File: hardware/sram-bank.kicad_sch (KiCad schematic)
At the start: 9 parts, among them U1 74LVC138A, U13 74LVC138A

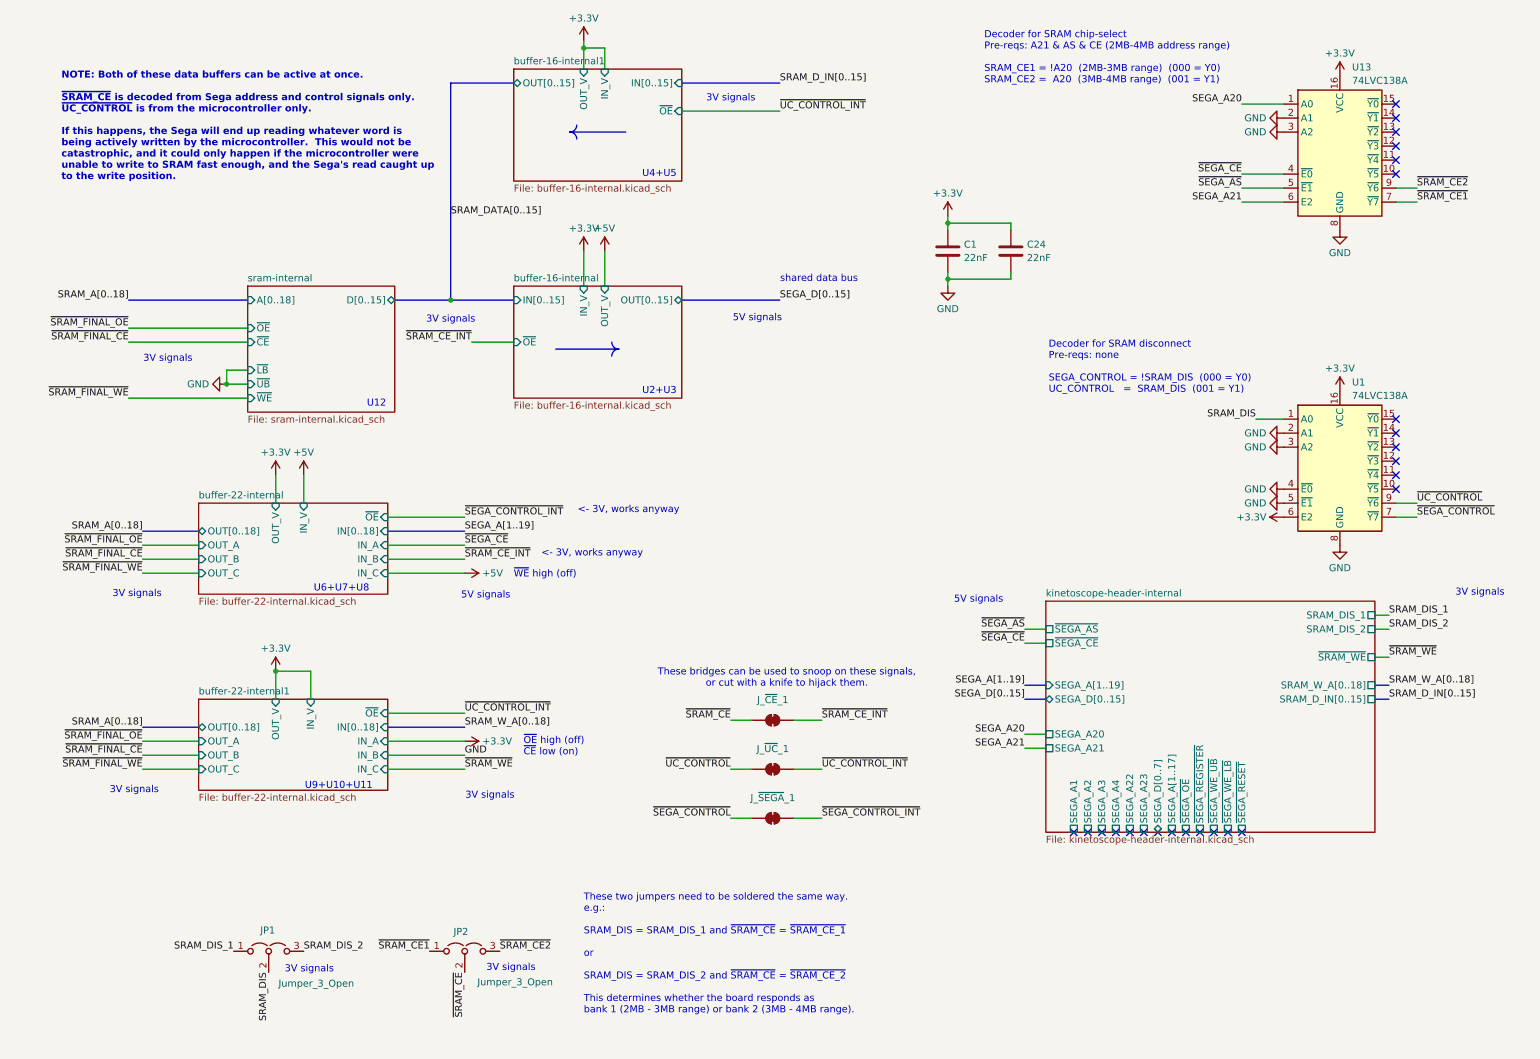
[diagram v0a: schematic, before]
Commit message: Fix SRAM bank hardware design
 - Fix SRAM OE line (was previously CE by accident)
 - Fix buffer OE line
 - Add test pads for ~{SEGA_OE}, ~{SRAM_WE}, ~{SRAM_FINAL_OE}
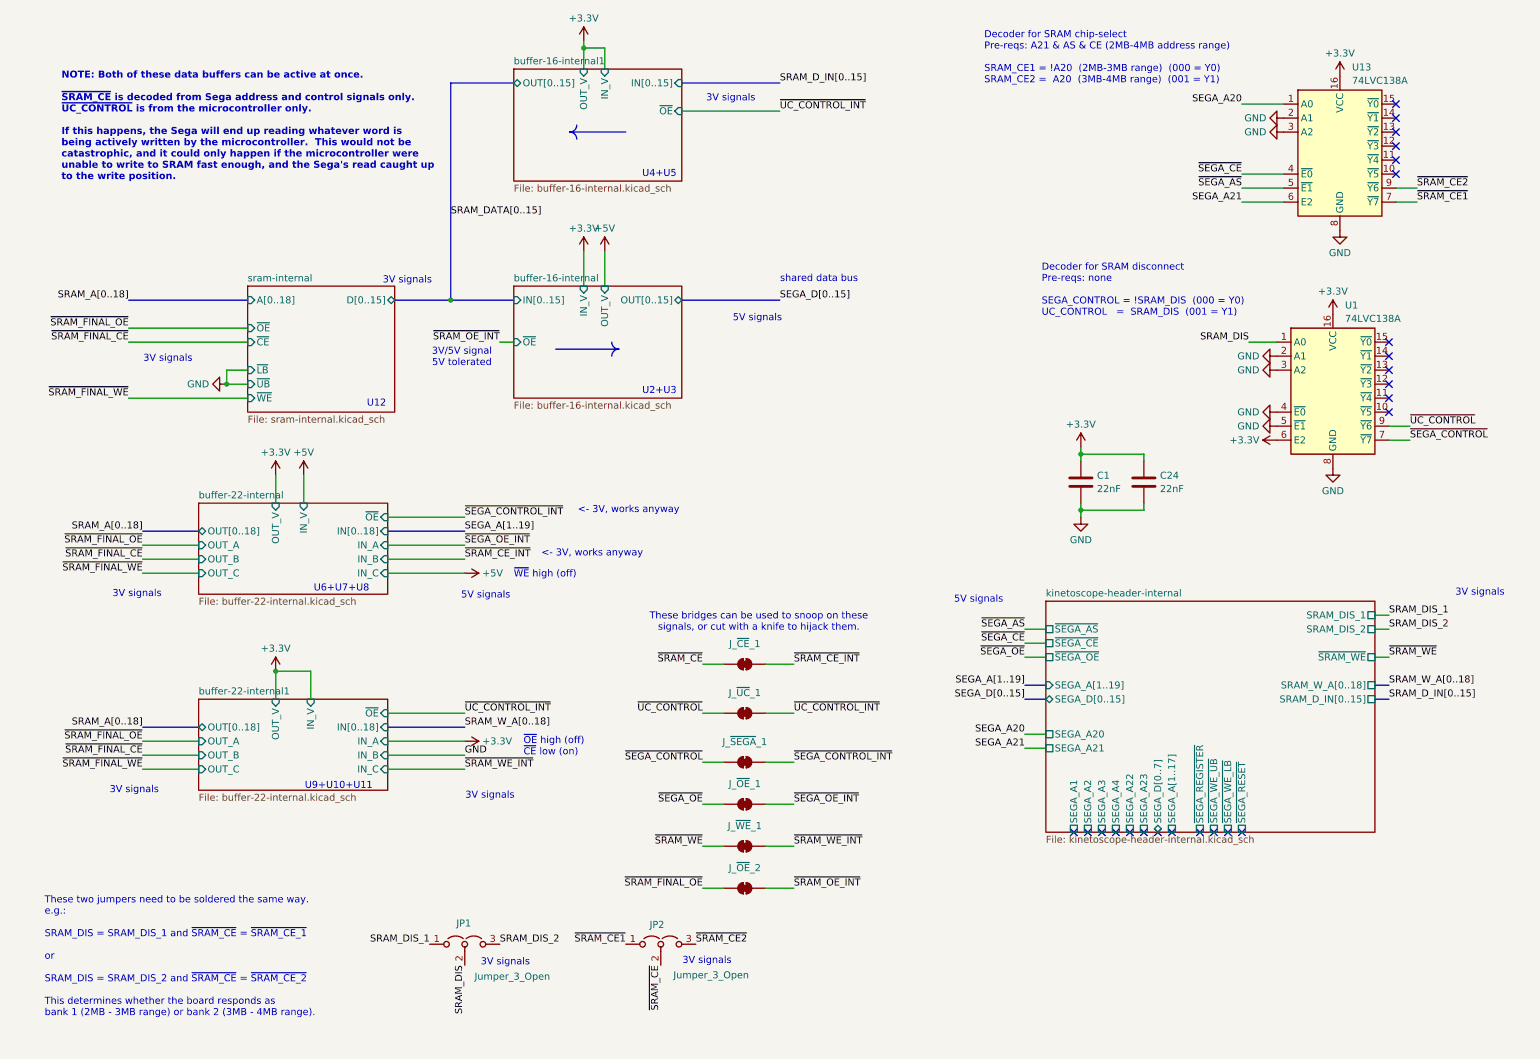
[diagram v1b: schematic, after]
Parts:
- added J_~{OE}_1, J_~{OE}_2, J_~{WE}_1: ~, Jumper:SolderJumper-2_P1.3mm_Bridged_RoundedPad1.0x1.5mm, symbol Jumper:SolderJumper_2_Bridged
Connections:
- net ~{SRAM_FINAL_OE}: now also J_~{OE}_2.1 (A)
- net ~{SRAM_WE}: now also J_~{WE}_1.1 (A)
- new net ~{SEGA_OE_INT}: J_~{OE}_1.2 (B)
- new net ~{SEGA_OE}: J_~{OE}_1.1 (A)
- new net ~{SRAM_OE_INT}: J_~{OE}_2.2 (B)
- new net ~{SRAM_WE_INT}: J_~{WE}_1.2 (B)
- no-connect marks 25 -> 24
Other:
- note added: "3V/5V signal 5V tolerated"
- moved on the sheet: C1, C24, JP1, JP2, J_~{CE}_1, J_~{SEGA}_1, J_~{UC}_1, U1

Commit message: Be consistent with SRAM bank numbering (0-1, not 1-2)
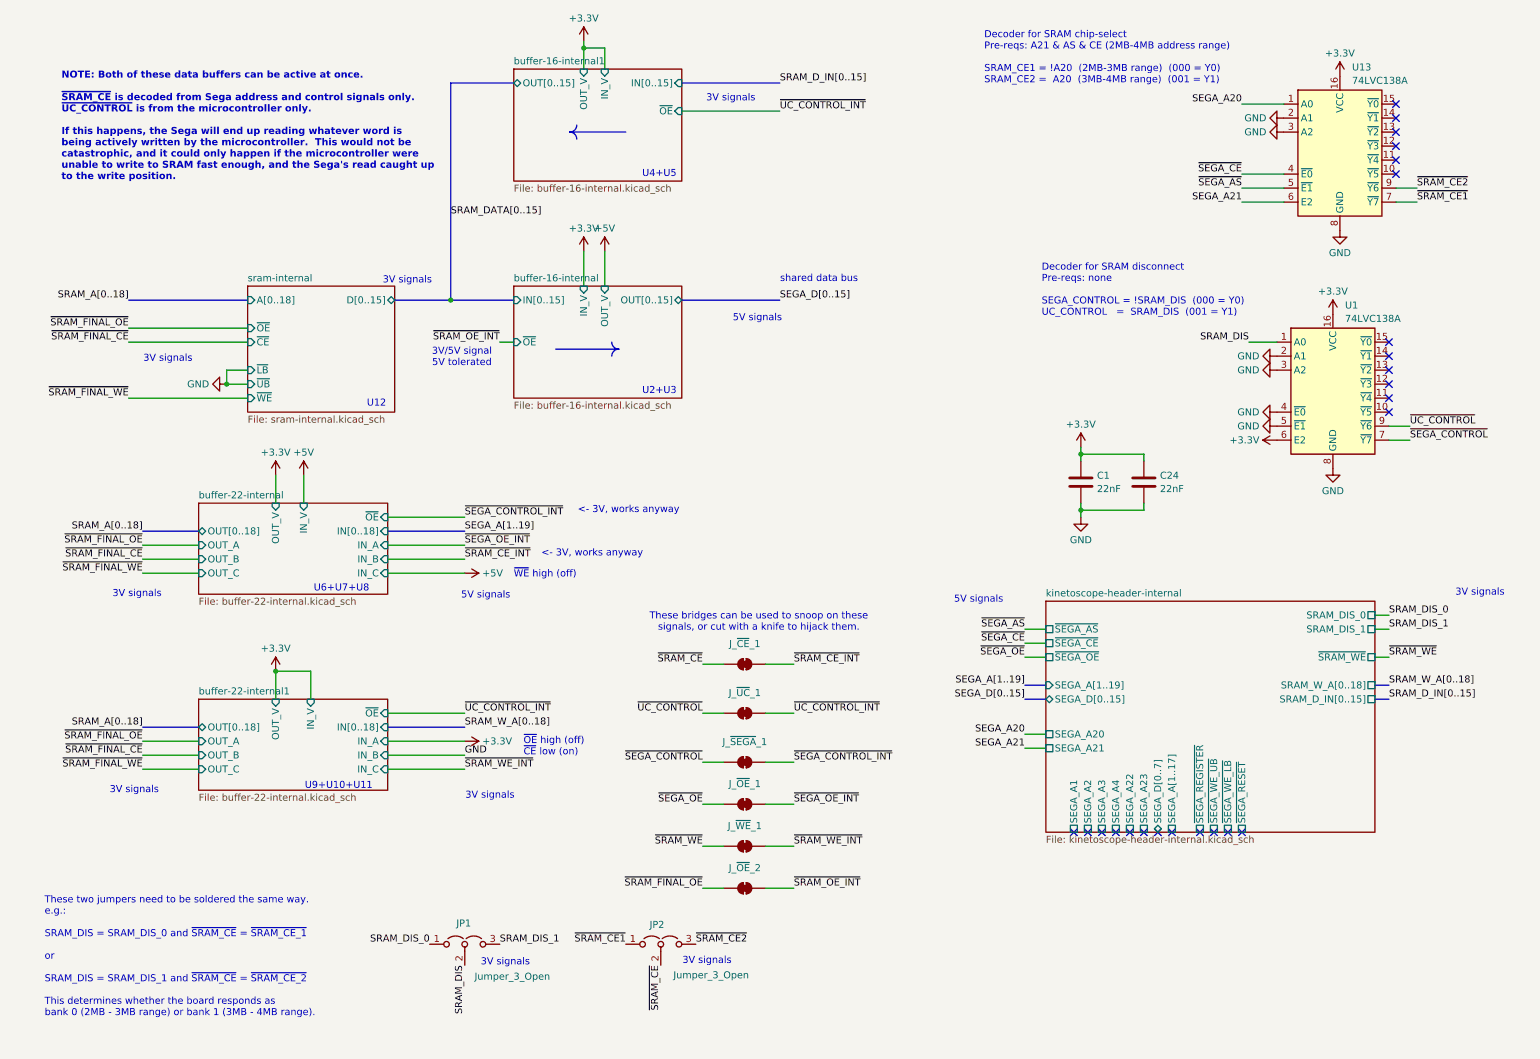
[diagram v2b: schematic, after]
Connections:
- net SRAM_DIS_2 is gone; now on net SRAM_DIS_1: JP1.3 (B)
- net SRAM_DIS_1: no longer JP1.1 (A)
- new net SRAM_DIS_0: JP1.1 (A)
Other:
- sheet kinetoscope-header-internal ports: added SRAM_DIS_0; removed SRAM_DIS_2
- note added: "These two jumpers need to be soldered the same way. e.g.: SRAM_DIS = SRAM_DIS_0 and ~{SRAM_CE} = ~{SRAM_CE_1} or SRAM_DIS = SRAM_DIS_1 and ~{SRAM_CE} = ~{SRAM_CE_2} This determines whether the board responds as bank 0 (2MB - 3MB range) or bank 1 (3MB - 4MB range)."
- note removed: "These two jumpers need to be soldered the same way. e.g.: SRAM_DIS = SRAM_DIS_1 and ~{SRAM_CE} = ~{SRAM_CE_1} or SRAM_DIS = SRAM_DIS_2 and ~{SRAM_CE} = ~{SRAM_CE_2} This determines whether the board responds as bank 1 (2MB - 3MB range) or bank 2 (3MB - 4MB range)."
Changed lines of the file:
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@@
 		)
 	)
-	(text "These two jumpers need to be soldered the same way.\ne.g.:\n\nSRAM_DIS = SRAM_DIS_1 and ~{SRAM_CE} = ~{SRAM_CE_1}\n\nor\n\nSRAM_DIS = SRAM_DIS_2 and ~{SRAM_CE} = ~{SRAM_CE_2}\n\nThis determines whether the board responds as\nbank 1 (2MB - 3MB range) or bank 2 (3MB - 4MB range)."
+	(text "These two jumpers need to be soldered the same way.\ne.g.:\n\nSRAM_DIS = SRAM_DIS_0 and ~{SRAM_CE} = ~{SRAM_CE_1}\n\nor\n\nSRAM_DIS = SRAM_DIS_1 and ~{SRAM_CE} = ~{SRAM_CE_2}\n\nThis determines whether the board responds as\nbank 0 (2MB - 3MB range) or bank 1 (3MB - 4MB range)."
 		(exclude_from_sim no)
 		(at 17.78 183.896 0)
@@
 		)
 	)
-	(label "SRAM_DIS_2"
+	(label "SRAM_DIS_1"
 		(at 261.62 124.46 0)
 		(fields_autoplaced yes)
@@
 		)
 	)
-	(label "SRAM_DIS_1"
+	(label "SRAM_DIS_0"
 		(at 261.62 121.92 0)
 		(fields_autoplaced yes)
@@
 		)
 	)
-	(label "SRAM_DIS_1"
+	(label "SRAM_DIS_0"
 		(at 87.63 181.61 180)
 		(fields_autoplaced yes)
@@
 		)
 	)
-	(label "SRAM_DIS_2"
+	(label "SRAM_DIS_1"
 		(at 100.33 181.61 0)
 		(fields_autoplaced yes)
@@
 			)
 		)
-		(pin "SRAM_DIS_2" passive
+		(pin "SRAM_DIS_1" passive
 			(at 259.08 124.46 0)
 			(effects
@@
 			)
 		)
-		(pin "SRAM_DIS_1" passive
+		(pin "SRAM_DIS_0" passive
 			(at 259.08 121.92 0)
 			(effects

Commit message: Fix SRAM bank design
 - Fix address decoders, Y0/Y1 and Y7/Y6 were flipped
 - SRAM_CE signal was insufficient, combined CE+OE needed
 - Buffer voltage at 5V meant 3.3V signals were too low, fixed to 3.3V
 - Update comments and add drawings

Only updates schematic.  PCB update will come in a later commit.
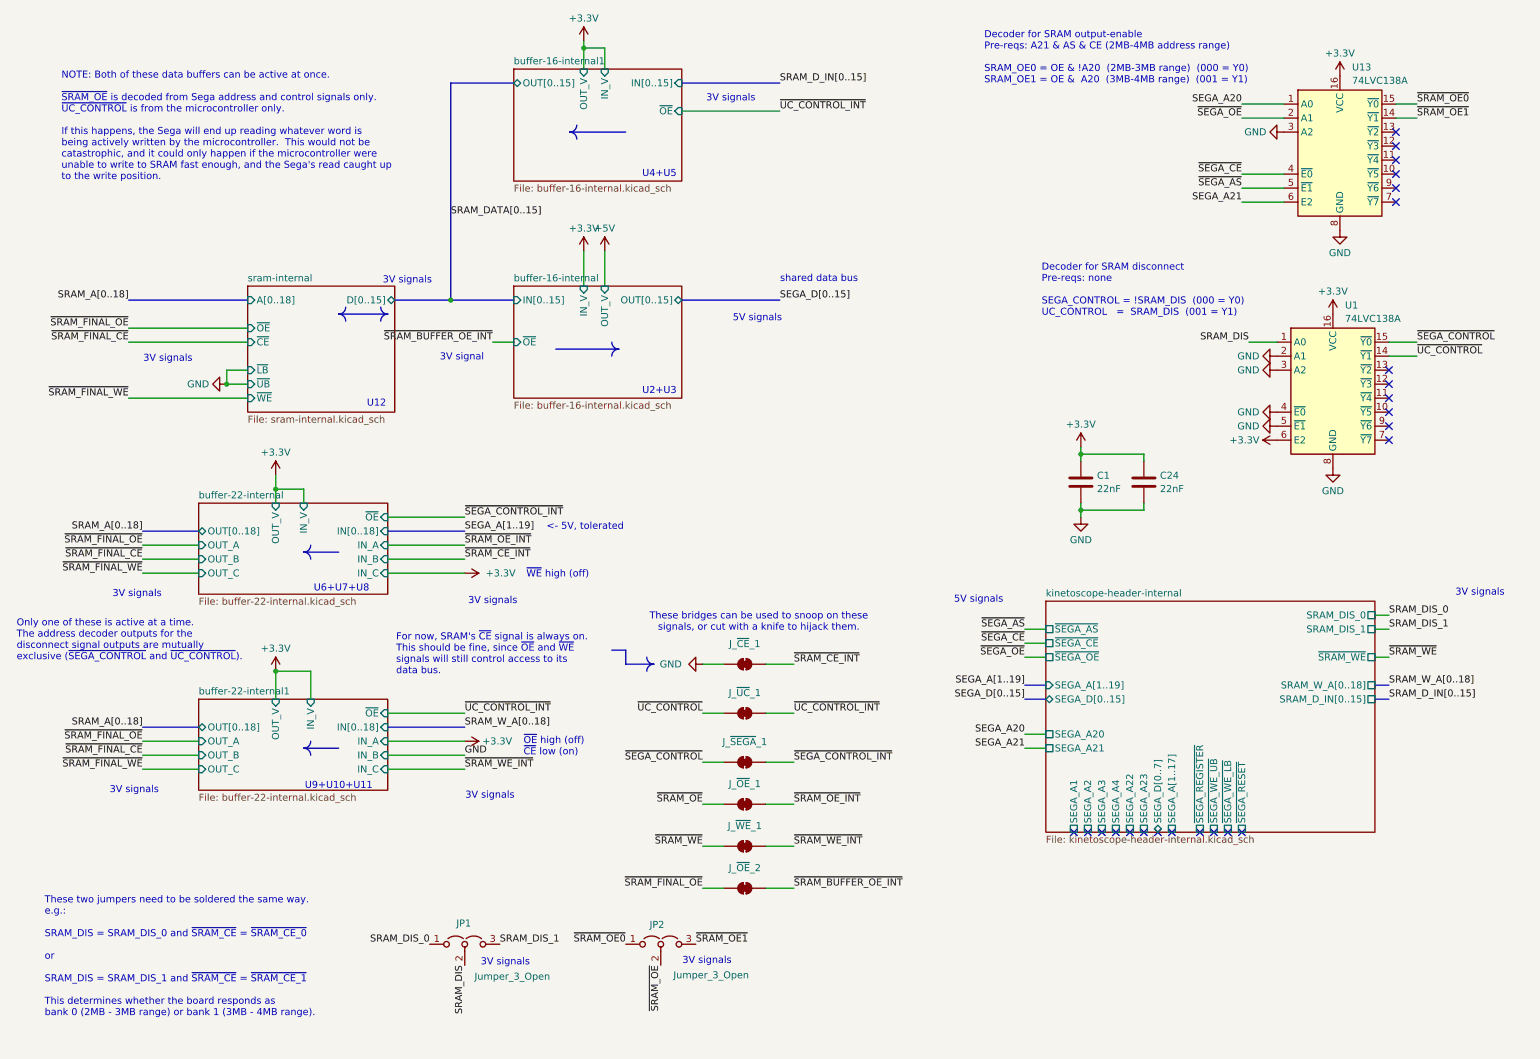
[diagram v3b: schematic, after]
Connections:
- net ~{SEGA_OE_INT} is gone; now on net ~{SRAM_OE_INT}: J_~{OE}_1.2 (B)
- net GND: now also J_~{CE}_1.1 (A); no longer U13.2 (A1)
- net ~{SEGA_CONTROL}: now also U1.15 (~{Y0}); no longer U1.7 (~{Y7})
- net ~{SEGA_OE}: now also U13.2 (A1); no longer J_~{OE}_1.1 (A)
- net ~{SRAM_OE_INT}: no longer J_~{OE}_2.2 (B)
- net ~{UC_CONTROL}: now also U1.14 (~{Y1}); no longer U1.9 (~{Y6})
- net ~{SRAM_OE1}: now reaches U13.14 (~{Y1})
- net ~{SRAM_OE1}: now also JP2.3 (B)
- net ~{SRAM_OE0}: now reaches U13.15 (~{Y0})
- net ~{SRAM_OE0}: now also JP2.1 (A)
- net ~{SRAM_CE1}: no longer names the net of U13.7 (~{Y7})
- net ~{SRAM_CE1}: no longer JP2.1 (A)
- net ~{SRAM_CE2}: no longer names the net of U13.9 (~{Y6})
- net ~{SRAM_CE2}: no longer JP2.3 (B)
- net ~{SRAM_CE} renamed ~{SRAM_OE}
- net ~{SRAM_OE}: now also J_~{OE}_1.1 (A); no longer J_~{CE}_1.1 (A)
- new net ~{SRAM_BUFFER_OE_INT}: J_~{OE}_2.2 (B)
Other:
- note added: "3V signal"
- note added: "<- 5V, tolerated"
- note added: "Decoder for SRAM output-enable Pre-reqs: A21 & AS & CE (2MB-4MB address range) SRAM_OE0 = OE & !A20 (2MB-3MB range) (000 = Y0) SRAM_OE1 = OE & A20 (3MB-4MB range) (001 = Y1)"
- note added: "For now, SRAM's ~{CE} signal is always on. This should be fine, since ~{OE} and ~{WE} signals will still control access to its data bus."
- note added: "NOTE: Both of these data buffers can be active at once. ~{SRAM_OE} is decoded from Sega address and control signals only. ~{UC_CONTROL} is from the microcontroller only. If this happens, the Sega will end up reading whatever word is being actively written by the microcontroller. This would not be catastrophic, and it could only happen if the microcontroller were unable to write to SRAM fast enoug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"
- note added: "Only one of these is active at a time. The address decoder outputs for the disconnect signal outputs are mutually exclusive (~{SEGA_CONTROL} and ~{UC_CONTROL})."
- note added: "These two jumpers need to be soldered the same way. e.g.: SRAM_DIS = SRAM_DIS_0 and ~{SRAM_CE} = ~{SRAM_CE_0} or SRAM_DIS = SRAM_DIS_1 and ~{SRAM_CE} = ~{SRAM_CE_1} This determines whether the board responds as bank 0 (2MB - 3MB range) or bank 1 (3MB - 4MB range)."
- note removed: "3V/5V signal 5V tolerated"
- note removed: "<- 3V, works anyway"
- note removed: "Decoder for SRAM chip-select Pre-reqs: A21 & AS & CE (2MB-4MB address range) SRAM_CE1 = !A20 (2MB-3MB range) (000 = Y0) SRAM_CE2 = A20 (3MB-4MB range) (001 = Y1)"
- note removed: "NOTE: Both of these data buffers can be active at once. ~{SRAM_CE} is decoded from Sega address and control signals only. ~{UC_CONTROL} is from the microcontroller only. If this happens, the Sega will end up reading whatever word is being actively written by the microcontroller. This would not be catastrophic, and it could only happen if the microcontroller were unable to write to SRAM fast enoug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"
- note removed: "These two jumpers need to be soldered the same way. e.g.: SRAM_DIS = SRAM_DIS_0 and ~{SRAM_CE} = ~{SRAM_CE_1} or SRAM_DIS = SRAM_DIS_1 and ~{SRAM_CE} = ~{SRAM_CE_2} This determines whether the board responds as bank 0 (2MB - 3MB range) or bank 1 (3MB - 4MB range)."
